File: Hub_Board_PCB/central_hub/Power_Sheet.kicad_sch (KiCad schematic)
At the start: 16 parts, among them J4 Barrel_Jack, U3 AP2112K-3.3TRG1, U4 AP63205WU-7

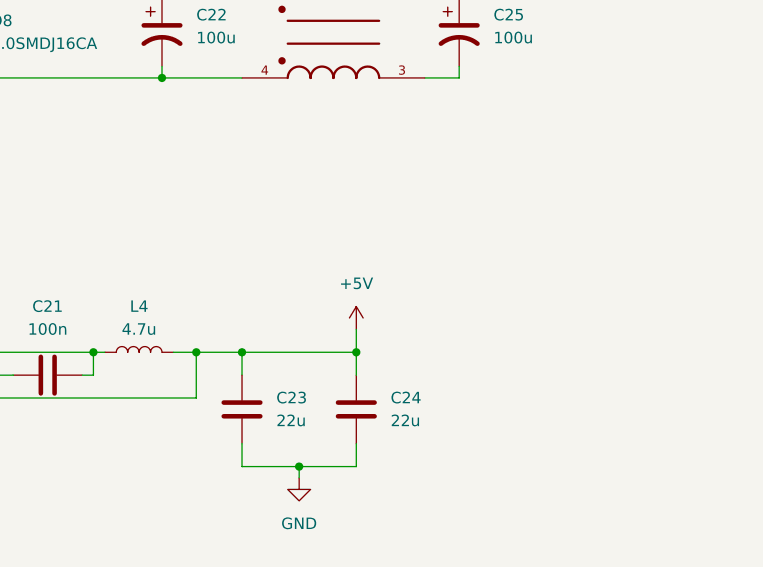
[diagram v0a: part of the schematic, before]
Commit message: - added global net-labels and reorganized pages - 4.0" TFT SPI 480*320 V2.1 display may already have a level-shifter (actually has HR2046, touch screen controller) so may not need to include voltage dividers and NMOSes
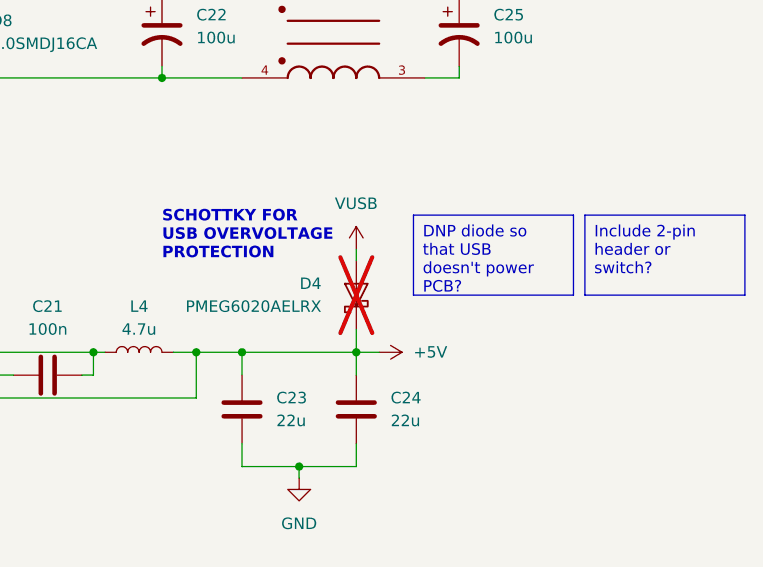
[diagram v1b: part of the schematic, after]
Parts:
- added D4: PMEG6020AELRX, Diode_SMD:Nexperia_CFP3_SOD-123W, symbol Diode:PMEG6020AELR
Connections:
- net +5V: now also D4.1 (K)
- new net VUSB: D4.2 (A)
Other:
- note added: "SCHOTTKY FOR USB OVERVOLTAGE PROTECTION"

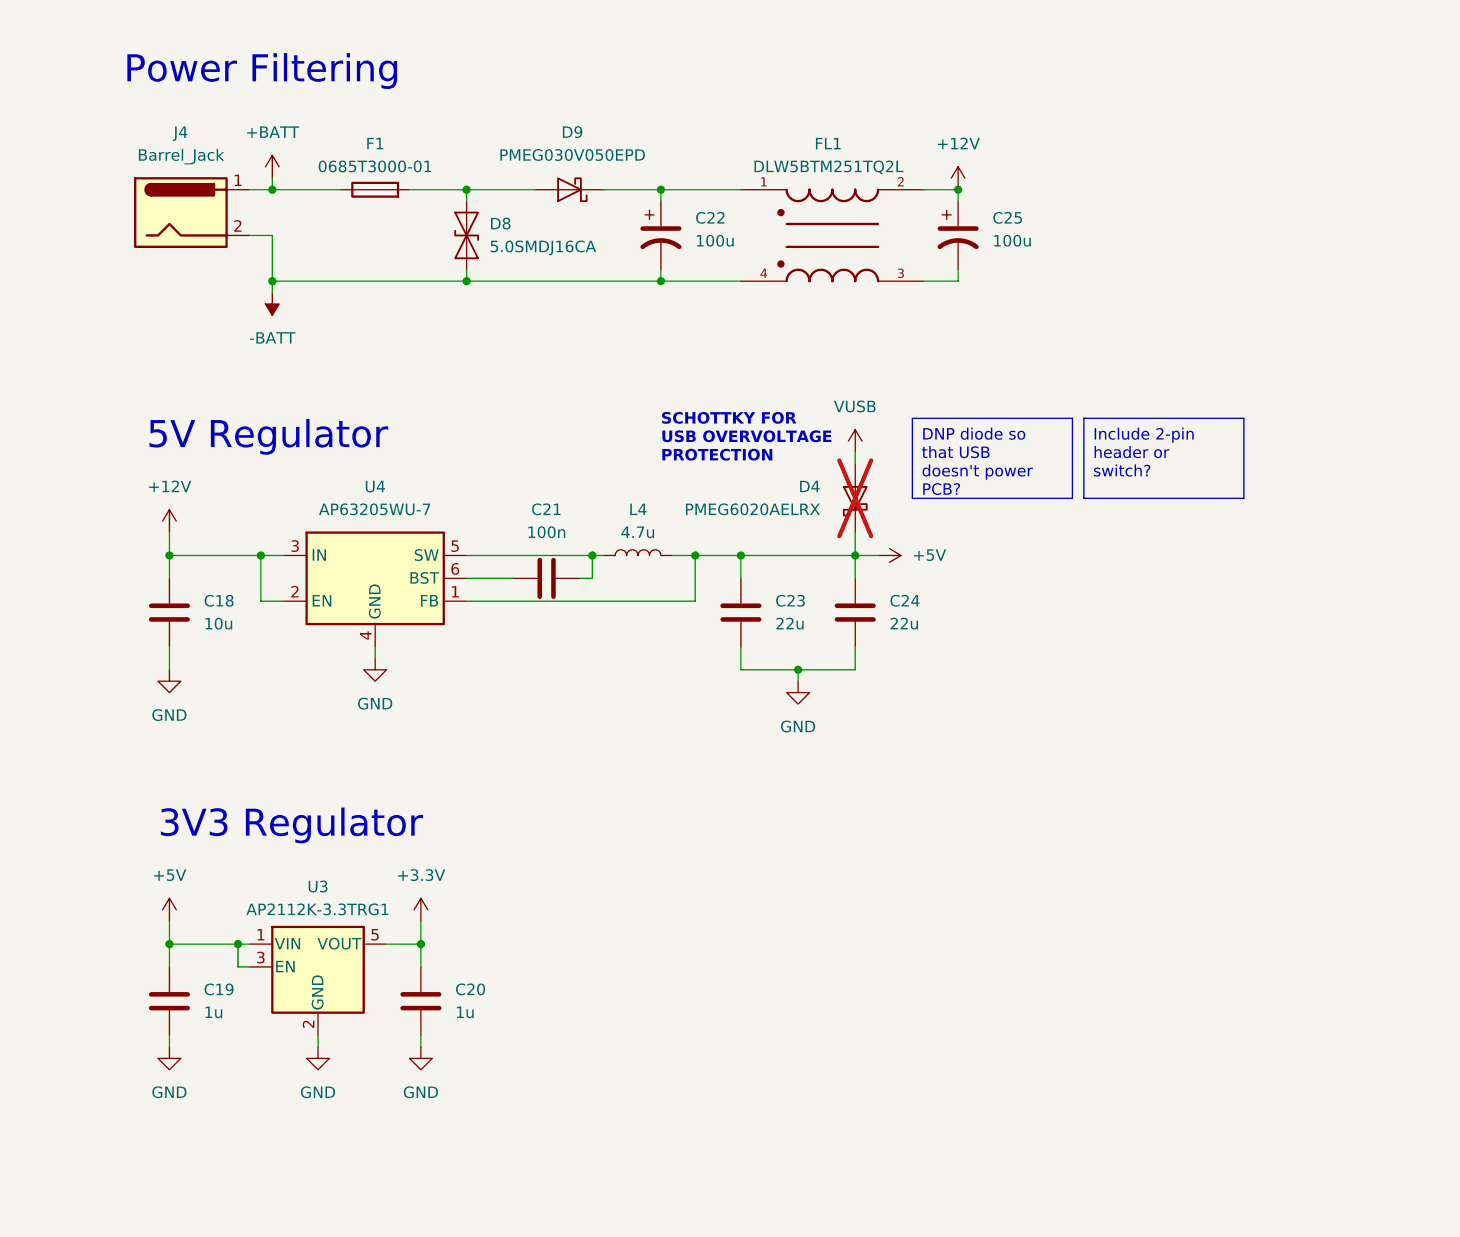
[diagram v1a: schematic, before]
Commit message: - added header for shorting VUSB and +5V
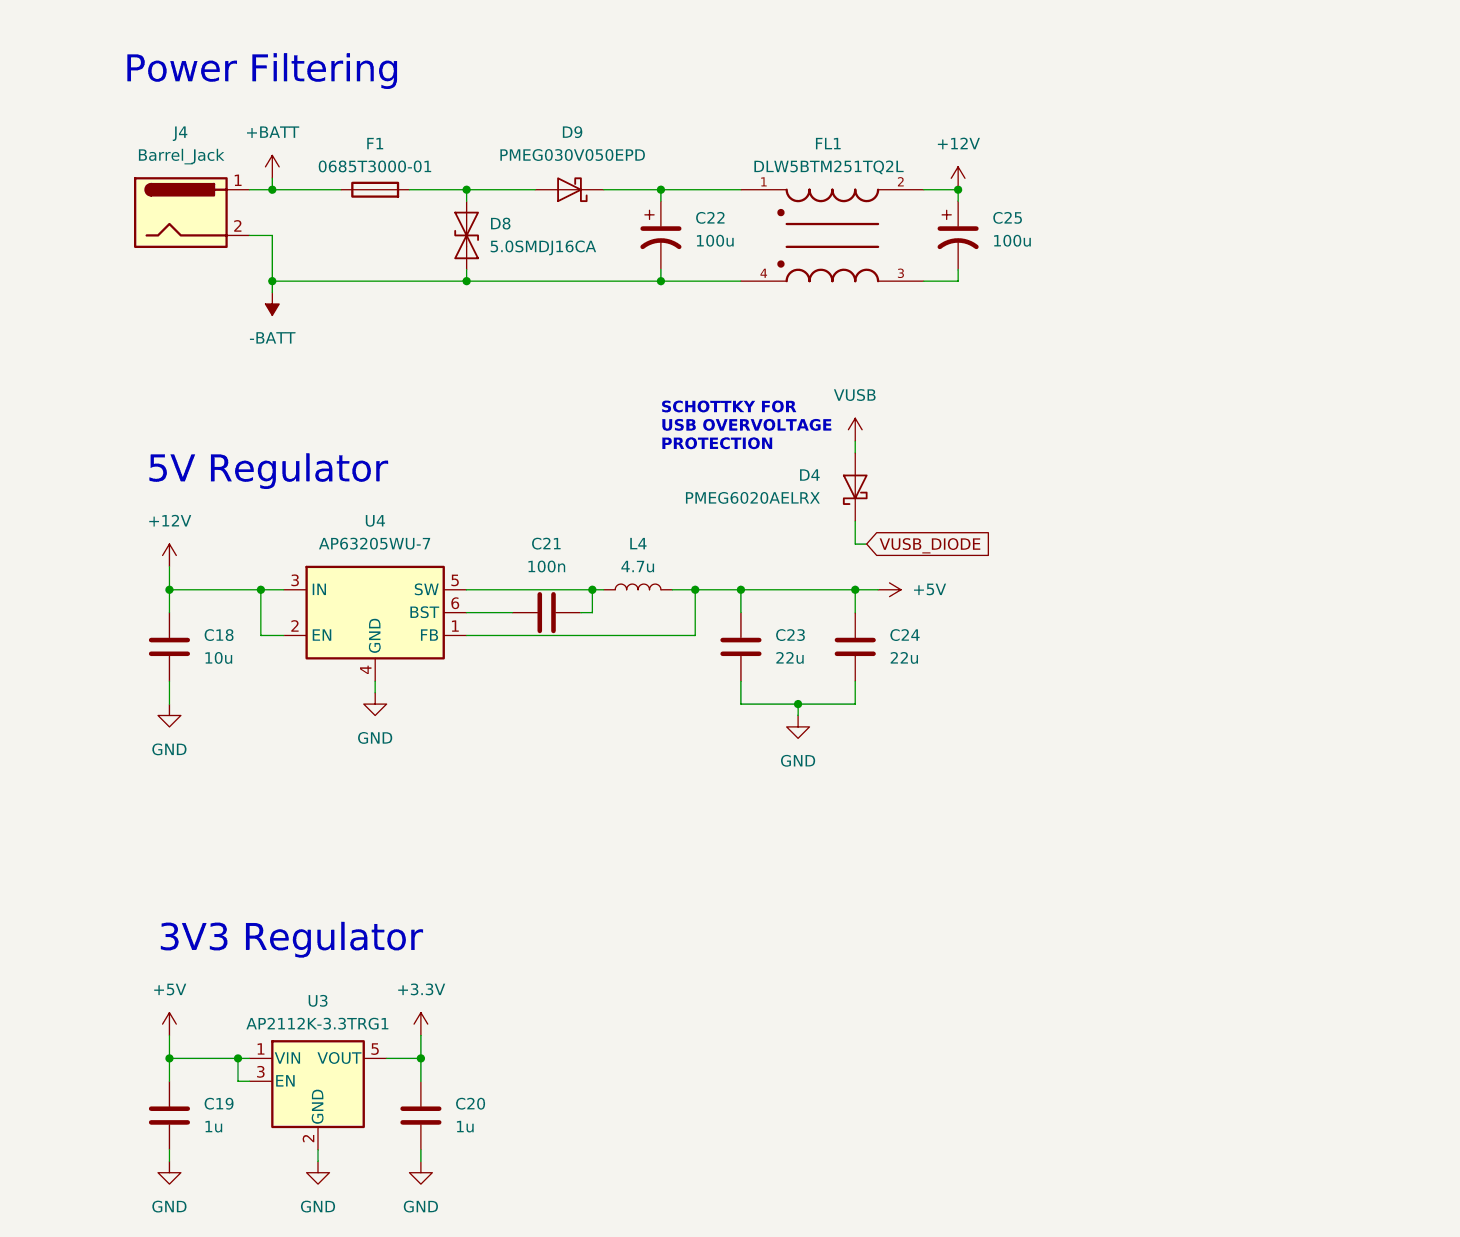
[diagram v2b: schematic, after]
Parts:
- D4: now fitted
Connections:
- net +5V: no longer D4.1 (K)
- new net VUSB_DIODE: D4.1 (K)
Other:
- moved on the sheet: C18, C19, C20, C21, C23, C24, L4, U3, U4

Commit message: Added footprints for almost all components
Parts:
- C15: renamed from C18; footprint (none) -> Capacitor_SMD:C_0603_1608Metric
- C16: renamed from C19; footprint (none) -> Capacitor_SMD:C_0603_1608Metric
- C17: renamed from C20; footprint (none) -> Capacitor_SMD:C_0603_1608Metric
- C18: renamed from C21; footprint (none) -> Capacitor_SMD:C_0603_1608Metric
- C19: renamed from C22; footprint (none) -> Capacitor_SMD:C_0603_1608Metric
- C20: renamed from C23; footprint (none) -> Capacitor_SMD:C_0603_1608Metric
- C21: renamed from C24; footprint (none) -> Capacitor_SMD:C_0603_1608Metric
- C22: renamed from C25; footprint (none) -> Capacitor_SMD:C_0603_1608Metric
- D8: footprint (none) -> Diode_SMD:D_0603_1608Metric
- F1: footprint (none) -> Fuse:Fuse_0603_1608Metric
- FL1: footprint DLW5BTM251TQ2L:FIL_DLW5BTM251TQ2L -> (none)
- J2: renamed from J4; footprint (none) -> Connector_BarrelJack:BarrelJack_CUI_PJ-063AH_Horizontal
- renumbered L4 to L3, U3 to U5, U4 to U6

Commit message: Added all other footprints... populated all components with NO errors or warnings :)
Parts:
- removed J2: Barrel_Jack, Connector_BarrelJack:BarrelJack_CUI_PJ-063AH_Horizontal, symbol Connector:Barrel_Jack
- added J2: Barrel_Jack_MountingPin, Connector_BarrelJack:BarrelJack_CUI_PJ-063AH_Horizontal, symbol Connector:Barrel_Jack_MountingPin
- FL1: footprint (none) -> ~ALL:FIL_DLW5BTZ251TQ2L
- L3: footprint (none) -> ~ALL:IND_VLS6045EX-100M
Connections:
- net +BATT: now also J2.1
- net -BATT: now also J2.2
- no-connect marks 0 -> 1
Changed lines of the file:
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@@
   (junction (at 68.58 144.78) (diameter 0) (color 0 0 0 0)
   )
+  (no_connect (at 41.91 58.42))
   (wire (pts (xy 104.14 105.41) (xy 110.49 105.41))
     (stroke (width 0) (type default))
@@
       (effects (font (size 1.27 1.27)))
     )
-    (property "Footprint" "" (at 114.3 53.34 0)
+    (property "Footprint" "~ALL:FIL_DLW5BTZ251TQ2L" (at 114.3 53.34 0)
       (effects (font (size 1.27 1.27)) (justify bottom) hide)
     )
@@
         (path "/a439ee58-92e3-49e0-a19d-7c5a25d23ba1"
           (reference "#PWR010") (unit 1)
-        )
-      )
-    )
-  )
-  (symbol (lib_id "Connector:Barrel_Jack") (at 41.91 50.8 0) (unit 1)
-    (in_bom yes) (on_board yes) (dnp no) (fields_autoplaced)
-    (property "Reference" "J2" (at 41.91 41.91 0)
-      (effects (font (size 1.27 1.27)))
-    )
-    (property "Value" "Barrel_Jack" (at 41.91 44.45 0)
-      (effects (font (size 1.27 1.27)))
-    )
-    (property "Footprint" "Connector_BarrelJack:BarrelJack_CUI_PJ-063AH_Horizontal" (at 43.18 51.816 0)
-      (effects (font (size 1.27 1.27)) hide)
-    )
-    (property "Datasheet" "~" (at 43.18 51.816 0)
-      (effects (font (size 1.27 1.27)) hide)
-    )
-    (pin "1")
-    (pin "2")
-    (instances
-      (project "central_hub"
-        (path "/0d9ec66e-0fbf-4d12-9b83-adf78971a00b/5d965db6-20f7-4bcf-a9c5-180dec6abb05"
-          (reference "J2") (unit 1)
-        )
-      )
-      (project "motor_board_pcb"
-        (path "/4ad82a24-c992-45c9-b523-12e12bcd6ced/8b03500d-82ba-403b-affc-552426d5b4ea"
-          (reference "J4") (unit 1)
-        )
-      )
-      (project "LocalDesign"
-        (path "/a439ee58-92e3-49e0-a19d-7c5a25d23ba1"
-          (reference "J1") (unit 1)
         )
       )
@@
     )
   )
+  (symbol (lib_id "Connector:Barrel_Jack_MountingPin") (at 41.91 50.8 0) (unit 1)
+    (in_bom yes) (on_board yes) (dnp no) (fields_autoplaced)
+    (property "Reference" "J2" (at 41.91 41.91 0)
+      (effects (font (size 1.27 1.27)))
+    )
+    (property "Value" "Barrel_Jack_MountingPin" (at 41.91 44.45 0)
+      (effects (font (size 1.27 1.27)))
+    )
+    (property "Footprint" "Connector_BarrelJack:BarrelJack_CUI_PJ-063AH_Horizontal" (at 43.18 51.816 0)
+      (effects (font (size 1.27 1.27)) hide)
+    )
+    (property "Datasheet" "~" (at 43.18 51.816 0)
+      (effects (font (size 1.27 1.27)) hide)
+    )
+    (pin "1")
+    (pin "2")
+    (pin "MP")
+    (instances
+      (project "central_hub"
+        (path "/0d9ec66e-0fbf-4d12-9b83-adf78971a00b/5d965db6-20f7-4bcf-a9c5-180dec6abb05"
+          (reference "J2") (unit 1)
+        )
+      )
+      (project "motor_board_pcb"
+        (path "/4ad82a24-c992-45c9-b523-12e12bcd6ced/8b03500d-82ba-403b-affc-552426d5b4ea"
+          (reference "J6") (unit 1)
+        )
+      )
+    )
+  )
   (symbol (lib_id "power:+3.3V") (at 68.58 142.24 0) (unit 1)
     (in_bom yes) (on_board yes) (dnp no) (fields_autoplaced)
@@
       (effects (font (size 1.27 1.27)))
     )
-    (property "Footprint" "" (at 92.71 92.71 0)
-      (effects (font (size 1.27 1.27)) hide)
-    )
+    (property "Footprint" "~ALL:IND_VLS6045EX-100M" (at 92.71 92.71 0)
+      (effects (font (size 1.27 1.27)) hide)
+    )
